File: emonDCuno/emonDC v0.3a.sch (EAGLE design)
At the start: 81 parts, among them Q1 16Mhz XT49M-2016M, U1_TQFP ATMEGA328P

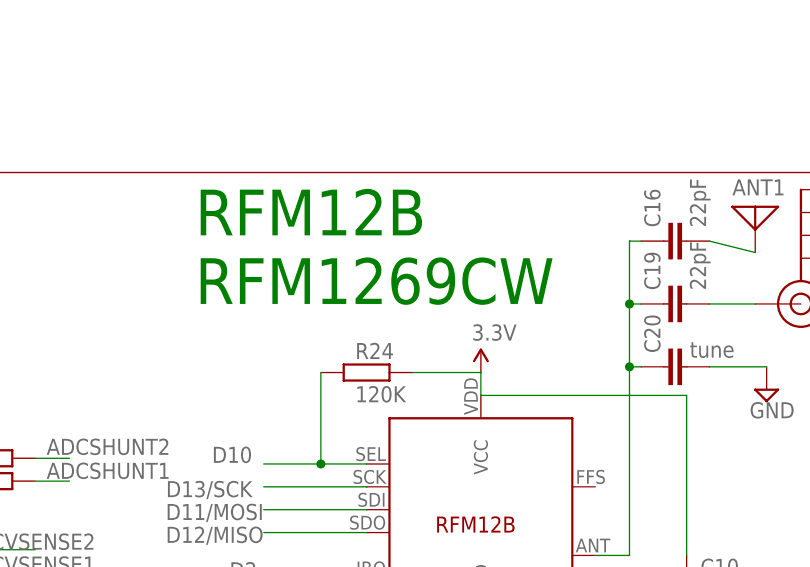
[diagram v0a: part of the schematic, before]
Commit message: RFM69 onto board
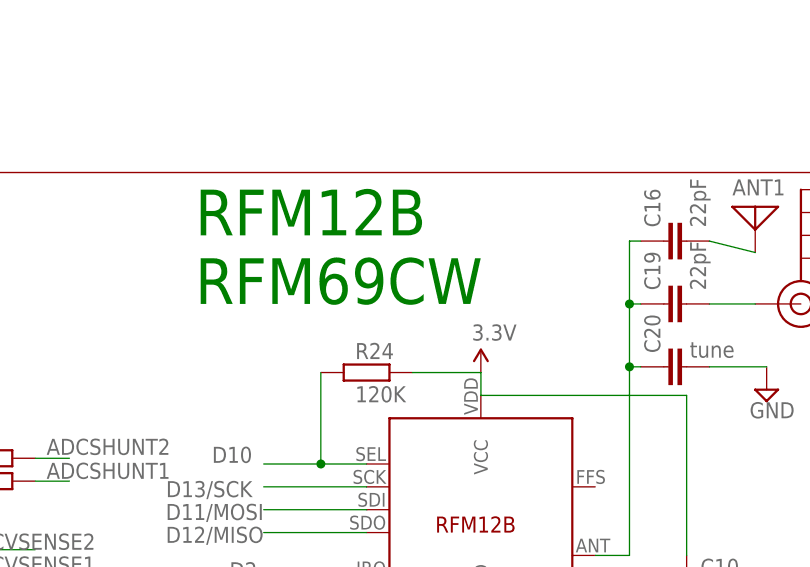
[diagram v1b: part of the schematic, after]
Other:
- note added: "RFM12B RFM69CW"
- note removed: "RFM12B RFM1269CW"
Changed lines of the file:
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@@
 <setting verticaltext="up"/>
 </settings>
-<grid distance="0.01" unitdist="inch" unit="inch" style="lines" multiple="1" display="yes" altdistance="0.01" altunitdist="inch" altunit="inch"/>
+<grid distance="0.1" unitdist="inch" unit="inch" style="lines" multiple="1" display="no" altdistance="0.01" altunitdist="inch" altunit="inch"/>
 <layers>
 <layer number="1" name="Top" color="4" fill="1" visible="no" active="no"/>
@@
 <text x="94.615" y="370.84" size="3.81" layer="91">ATmega328</text>
 <text x="173.99" y="379.095" size="5.08" layer="91">RFM12B
-RFM1269CW</text>
+RFM69CW</text>
 <text x="263.144" y="377.063" size="2.54" layer="91">DIP
 Switch</text>
